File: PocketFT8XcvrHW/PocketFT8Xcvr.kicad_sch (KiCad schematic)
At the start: 59 parts, among them J1 HX8357D SPI, J2 22-23-2021, J3 B5B-XH-A_LF__SN_, J4 XMT PWR, J5 HX8357D 8-BIT, Q3 2N7000, U1 MCP3422A1T-E/SN, U2 Si4735-D60-GU, U3 SN74ACT244DWR, U4 SI5351C-B-GM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

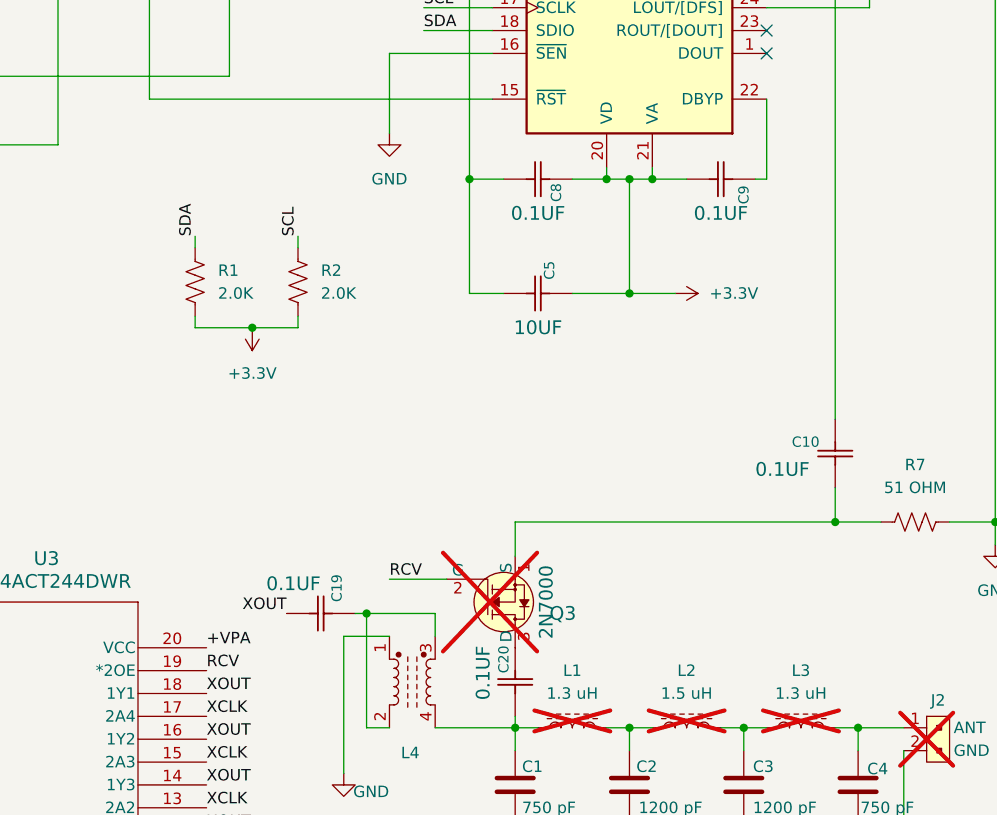
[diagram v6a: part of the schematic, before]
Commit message: REPLACED the two 2N7000s with a dual mosfet, 2N7002DW
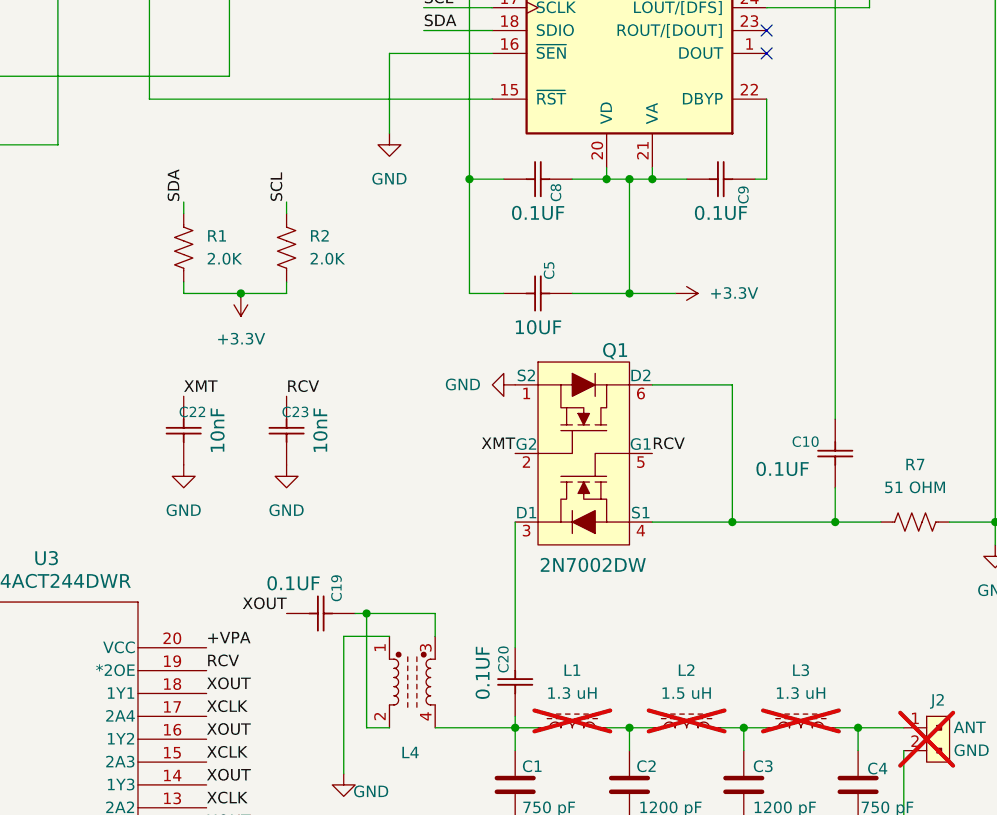
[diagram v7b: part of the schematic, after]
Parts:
- added C22, C23: 10nF, Capacitor_SMD:C_0603_1608Metric, symbol Kemet2024-08-02_22-05-35:C0603C104K4RACTU
- Q1: renamed from Q3; value 2N7000 -> 2N7002DW; footprint digikey-footprints:TO-92-3 -> digikey-footprints:SOT-363; symbol dk_Transistors-FETs-MOSFETs-Single:2N7000 -> dk_Transistors-FETs-MOSFETs-Arrays:2N7002DW; DK_Datasheet_Link https://www.onsemi.com/pub/Collateral/NDS7002A-D.PDF -> https://www.onsemi.com/pub/Collateral/2N7002DW-D.PDF; DK_Detail_Page /product-detail/en/on-semiconductor/2N7000/2N7000FS-ND/2442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 -> /product-detail/en/on-semiconductor/2N7002DW/2N7002DWCT-ND/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; Description_1 MOSFET N-CH 60V 200MA TO-92 -> MOSFET 2N-CH 60V 0.115A SC70-6; Digi-Key_PN 2N7000FS-ND -> 2N7002DWCT-ND; Family Transistors - FETs, MOSFETs - Single -> Transistors - FETs, MOSFETs - Arrays; MPN 2N7000 -> 2N7002DW; Mfg Part # 2N7000 -> 2N7002DW; Type THT -> SMT; now fitted; now in the parts list
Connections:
- net GND: now also Q1.1 (S2), C22.1, C23.1
- net RCV: now also Q1.5 (G1), C23.2; no longer Q1.2 (G)
- net XMT: now also Q1.2 (G2), C22.2
- net at C10.1, R7.2: now also Q1.4 (S1), Q1.6 (D2); no longer Q1.1 (S)
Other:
- moved on the sheet: R1, R2

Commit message: Added test points
Don't use sparkfun TPs again :(
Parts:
- added TP1, TP2, TP3, TP4: PTH, SparkFun-Connector:1x01, symbol SparkFun-Connector:TestPoint_PTH
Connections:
- net RCLK: now also TP3.1
- net XCLK: now also TP2.1
- net at C11.2, C6.1, R3.2: now also TP4.1
- net at U4.6 (CLKIN), Y1.3 (OUTPUT): now also TP1.1
